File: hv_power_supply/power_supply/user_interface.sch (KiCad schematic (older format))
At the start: 22 parts, among them J1 CONN_01x04, J2 CONN_02X03, J3 UF_5_VT, J4 UF_5_VT, J5 UF_5_VT, U3 ATMEGA16M1, Y1 Crystal_SMD

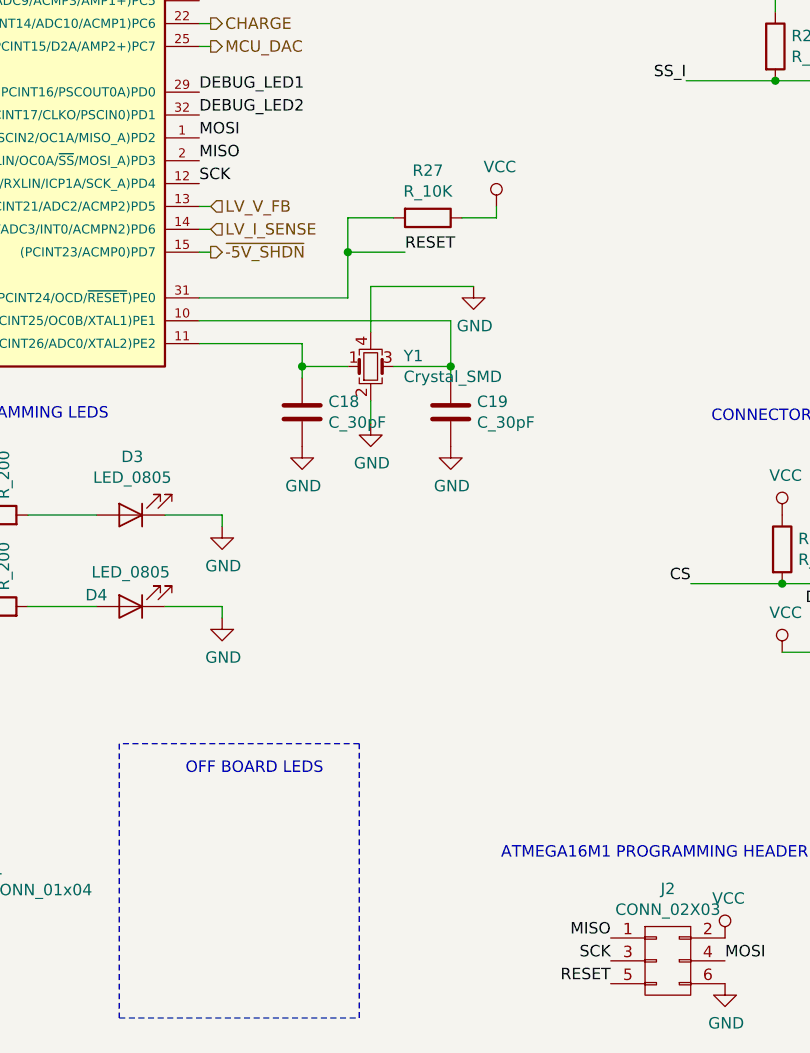
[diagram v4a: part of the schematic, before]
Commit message: All routing finished except for 5V and GND... Need to look into adding input filtering to power supply chips and some GND separation between LV, Flyback, and HV
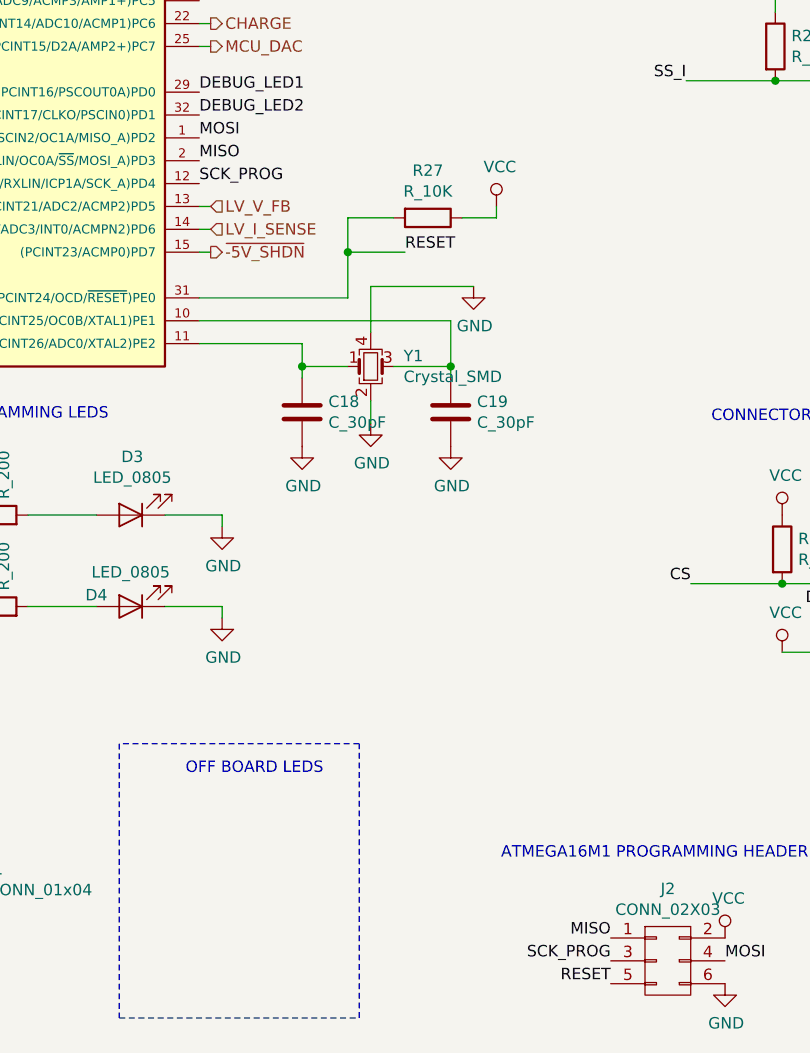
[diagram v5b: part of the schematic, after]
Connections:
- net SCK: no longer J2.3 (P3), U3.12 ((PCINT20/ADC1/RXD/RXLIN/ICP1A/SCK_A)PD4)
- new net SCK_PROG: J2.3 (P3), U3.12 ((PCINT20/ADC1/RXD/RXLIN/ICP1A/SCK_A)PD4)
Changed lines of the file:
@@
 MISO
 Text Label 5500 7100 2    50   ~ 0
-SCK
+SCK_PROG
 Text Label 5500 7200 2    50   ~ 0
 RESET
@@
 MOSI
 Text Label 3700 3700 0    50   ~ 0
-SCK
+SCK_PROG
 Text Label 3700 2000 0    50   ~ 0
 D_OUTPUT_V
